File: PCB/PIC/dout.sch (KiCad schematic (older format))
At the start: 67 parts, among them J10 TB_1X3, J11 TB_1X2, J12 TB_1X3, J13 TB_1X3, J14 TB_1X2, J15 TB_1X3, K1 RELAY_G5V-2, K2 RELAY_G5V-2, K3 RELAY_G5V-2, K4 RELAY_G5V-2, Q11 NDS7002A, Q12 NDS7002A, Q2 FQT13N06L, Q3 FQT13N06L, Q4 FQT13N06L, Q5 FQT13N06L, Q6 NDS7002A, Q7 NDS7002A, U23 MCP1416, U27 MCP1416, U28 MCP1416, U29 MCP1416

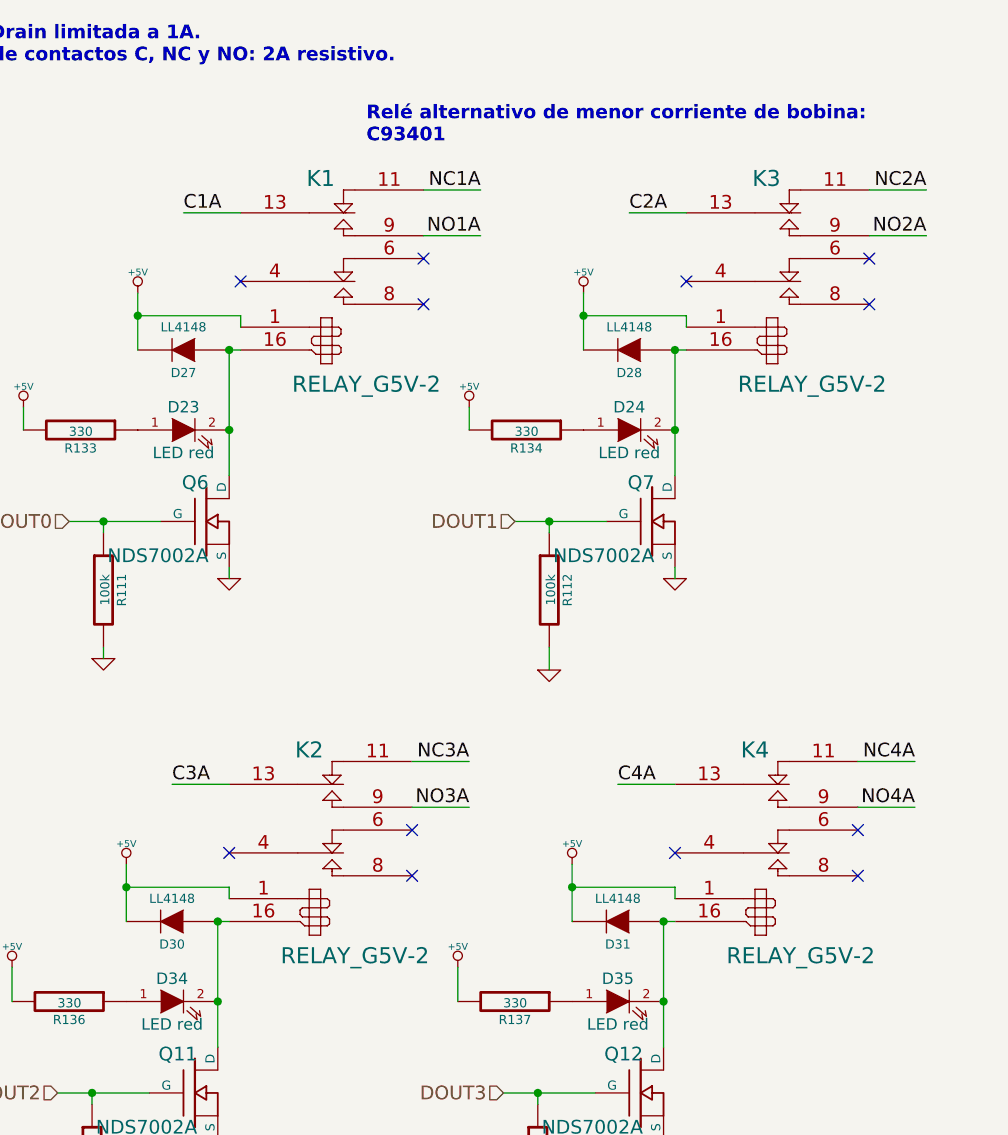
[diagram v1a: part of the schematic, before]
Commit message: cambio reles salida digital CIAA-PIC
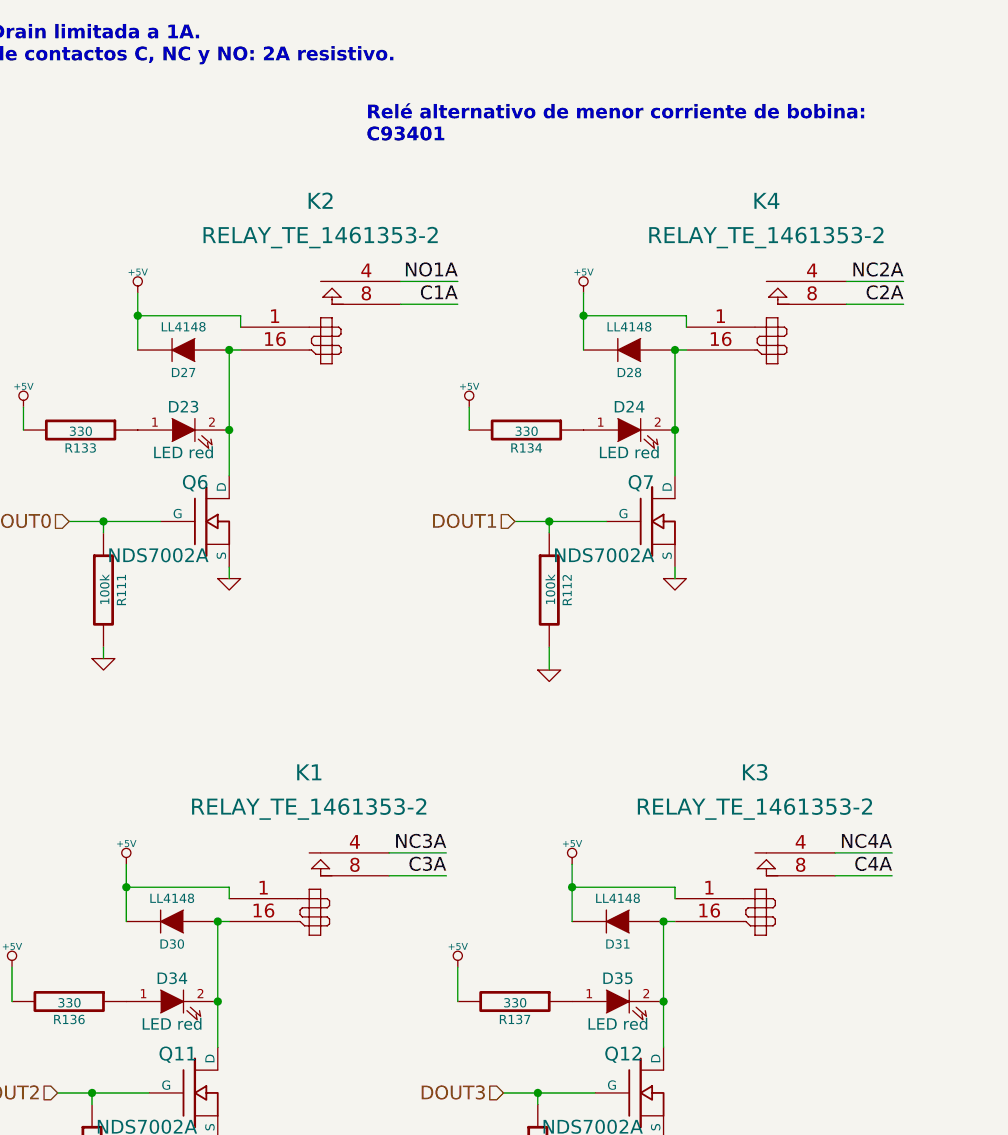
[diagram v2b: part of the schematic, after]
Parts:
- removed K1, K2, K3, K4: RELAY_G5V-2, footprints:G5V-2, symbol RELAY_G5V-2
- added K1, K2, K3, K4: RELAY_TE_1461353-2, footprints:1461353-2, symbol RELAY_TE_1461353-2
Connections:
- net +5V: now also K1.1, K2.1, K3.1, K4.1
- net C1A: now also K2.8 (T1)
- net C2A: now also K4.8 (T1)
- net C3A: now also K1.8 (T1)
- net C4A: now also K3.8 (T1)
- net NC2A: now also K4.4 (C1)
- net NC3A: now also K1.4 (C1)
- net NC4A: now also K3.4 (C1)
- net NO1A: now also K2.4 (C1)
- net at D23.2 (K), D27.1 (A), Q6.D: now also K2.16
- net at D30.1 (A), D34.2 (K), Q11.D: now also K1.16
- net at D24.2 (K), D28.1 (A), Q7.D: now also K4.16
- net at D31.1 (A), D35.2 (K), Q12.D: now also K3.16
- no-connect marks 12 -> 0
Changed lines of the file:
@@
 	0    -1   -1   0
 $EndComp
-Text Label 7650 1550 0    60   ~ 0
+Text Label 8850 1950 2    60   ~ 0
 C1A
-Text Label 8950 1450 2    60   ~ 0
-NC1A
-Text Label 8950 1650 2    60   ~ 0
+Text Label 8850 1850 2    60   ~ 0
 NO1A
 $Comp
@@
 	1    0    0    -1
 $EndComp
-Text Label 7600 4050 0    60   ~ 0
+Text Label 8800 4450 2    60   ~ 0
 C3A
-Text Label 8900 3950 2    60   ~ 0
+Text Label 8800 4350 2    60   ~ 0
 NC3A
-Text Label 8900 4150 2    60   ~ 0
-NO3A
 $Comp
 L MOSFET_N Q7
@@
 	1    0    0    -1
 $EndComp
-Text Label 9600 1550 0    60   ~ 0
+Text Label 10800 1950 2    60   ~ 0
 C2A
-Text Label 10900 1450 2    60   ~ 0
+Text Label 10800 1850 2    60   ~ 0
 NC2A
-Text Label 10900 1650 2    60   ~ 0
-NO2A
 $Comp
 L MOSFET_N Q12
@@
 	1    0    0    -1
 $EndComp
-Text Label 9550 4050 0    60   ~ 0
+Text Label 10750 4450 2    60   ~ 0
 C4A
-Text Label 10850 3950 2    60   ~ 0
+Text Label 10750 4350 2    60   ~ 0
 NC4A
-Text Label 10850 4150 2    60   ~ 0
-NO4A
 $Comp
 L THERMISTOR TH3
@@
 	3250 3200 3250 3150
 Wire Wire Line
-	7650 1550 7900 1550
-Wire Wire Line
-	8700 1450 8950 1450
-Wire Wire Line
-	8700 1650 8950 1650
+	8850 1950 8600 1950
+Wire Wire Line
+	8600 1850 8850 1850
 Wire Wire Line
 	7400 4400 7400 4650
@@
 Connection ~ 7250 5400
 Wire Wire Line
-	7600 4050 7850 4050
-Wire Wire Line
-	8650 3950 8900 3950
-Wire Wire Line
-	8650 4150 8900 4150
+	8800 4450 8550 4450
+Wire Wire Line
+	8550 4350 8800 4350
 Wire Wire Line
 	9400 1900 9400 2150
@@
 Connection ~ 9250 2900
 Wire Wire Line
-	9600 1550 9850 1550
-Wire Wire Line
-	10650 1450 10900 1450
-Wire Wire Line
-	10650 1650 10900 1650
+	10800 1950 10550 1950
+Wire Wire Line
+	10550 1850 10800 1850
 Wire Wire Line
 	9350 4400 9350 4650
@@
 Connection ~ 9200 5400
 Wire Wire Line
-	9550 4050 9800 4050
-Wire Wire Line
-	10600 3950 10850 3950
-Wire Wire Line
-	10600 4150 10850 4150
+	10750 4450 10500 4450
+Wire Wire Line
+	10500 4350 10750 4350
 Wire Wire Line
 	1050 5350 1750 5350
@@
 	1    0    0    -1
 $EndComp
-$Comp
-L RELAY_G5V-2 K1
-U 1 1 56AFD9BD
-P 8300 1800
-F 0 "K1" H 8250 2200 70  0000 C CNN
-F 1 "RELAY_G5V-2" H 8450 1300 70  0000 C CNN
-F 2 "footprints:G5V-2" H 7950 2300 60  0001 C CNN
-F 3 "http://www.digikey.hk/product-detail/en/omron-electronics-inc-emc-div/G5V-2-H1-DC24/Z110-ND/277846" H 8550 2550 60  0001 C CNN
-F 4 "G5V-2-DC5" H 8300 1800 60  0001 C CNN "manf#"
-	1    8300 1800
-	1    0    0    -1
-$EndComp
-$Comp
-L RELAY_G5V-2 K3
-U 1 1 56AFD9D4
-P 10250 1800
-F 0 "K3" H 10200 2200 70  0000 C CNN
-F 1 "RELAY_G5V-2" H 10400 1300 70  0000 C CNN
-F 2 "footprints:G5V-2" H 9650 2250 60  0001 C CNN
-F 3 "http://www.digikey.hk/product-detail/en/omron-electronics-inc-emc-div/G5V-2-H1-DC24/Z110-ND/277846" H 8550 2450 60  0001 C CNN
-F 4 "G5V-2-DC5" H 10250 1800 60  0001 C CNN "manf#"
-	1    10250 1800
-	1    0    0    -1
-$EndComp
-$Comp
-L RELAY_G5V-2 K4
-U 1 1 56AFD9E4
-P 10200 4300
-F 0 "K4" H 10150 4700 70  0000 C CNN
-F 1 "RELAY_G5V-2" H 10350 3800 70  0000 C CNN
-F 2 "footprints:G5V-2" H 10350 3700 60  0001 C CNN
-F 3 "http://www.digikey.hk/product-detail/en/omron-electronics-inc-emc-div/G5V-2-H1-DC24/Z110-ND/277846" H 8550 2150 60  0001 C CNN
-F 4 "G5V-2-DC5" H 10200 4300 60  0001 C CNN "manf#"
-	1    10200 4300
-	1    0    0    -1
-$EndComp
-$Comp
-L RELAY_G5V-2 K2
-U 1 1 56AFD9EA
-P 8250 4300
-F 0 "K2" H 8200 4700 70  0000 C CNN
-F 1 "RELAY_G5V-2" H 8400 3800 70  0000 C CNN
-F 2 "footprints:G5V-2" H 8400 3700 60  0001 C CNN
-F 3 "http://www.digikey.hk/product-detail/en/omron-electronics-inc-emc-div/G5V-2-H1-DC24/Z110-ND/277846" H 8550 2250 60  0001 C CNN
-F 4 "G5V-2-DC5" H 8250 4300 60  0001 C CNN "manf#"
-	1    8250 4300
-	1    0    0    -1
-$EndComp
 Wire Wire Line
 	7450 2000 7900 2000
@@
 Wire Wire Line
 	6900 4850 6900 5000
-NoConn ~ 8650 4250
-NoConn ~ 8650 4450
-NoConn ~ 10600 4250
-NoConn ~ 10600 4450
-NoConn ~ 7900 1850
-NoConn ~ 8700 1750
-NoConn ~ 8700 1950
-NoConn ~ 9850 1850
-NoConn ~ 10650 1750
-NoConn ~ 10650 1950
-NoConn ~ 7850 4350
-NoConn ~ 9800 4350
 Wire Wire Line
 	4000 1000 4000 2450
@@
 Wire Wire Line
 	4000 2450 4200 2450
+$Comp
+L RELAY_TE_1461353-2 K2
+U 1 1 57C69C4D
+P 8300 1800
+F 0 "K2" H 8250 2100 70  0000 C CNN
+F 1 "RELAY_TE_1461353-2" H 8250 1950 70  0000 C CNN
+F 2 "footprints:1461353-2" H 8200 1800 60  0001 C CNN
+F 3 "" H 8200 1800 60  0000 C CNN
+F 4 "1461353-2" H 8300 1800 60  0001 C CNN "manf#"
+	1    8300 1800
+	1    0    0    -1
+$EndComp
+$Comp
+L RELAY_TE_1461353-2 K4
+U 1 1 57C6B233
+P 10250 1800
+F 0 "K4" H 10200 2100 70  0000 C CNN
+F 1 "RELAY_TE_1461353-2" H 10200 1950 70  0000 C CNN
+F 2 "footprints:1461353-2" H 10150 1800 60  0001 C CNN
+F 3 "" H 10150 1800 60  0000 C CNN
+F 4 "1461353-2" H 10250 1800 60  0001 C CNN "manf#"
+	1    10250 1800
+	1    0    0    -1
+$EndComp
+$Comp
+L RELAY_TE_1461353-2 K3
+U 1 1 57C6BEA9
+P 10200 4300
+F 0 "K3" H 10150 4600 70  0000 C CNN
+F 1 "RELAY_TE_1461353-2" H 10150 4450 70  0000 C CNN
+F 2 "footprints:1461353-2" H 10100 4300 60  0001 C CNN
+F 3 "" H 10100 4300 60  0000 C CNN
+F 4 "1461353-2" H 10200 4300 60  0001 C CNN "manf#"
+	1    10200 4300
+	1    0    0    -1
+$EndComp
+$Comp
+L RELAY_TE_1461353-2 K1
+U 1 1 57C6C983
+P 8250 4300
+F 0 "K1" H 8200 4600 70  0000 C CNN
+F 1 "RELAY_TE_1461353-2" H 8200 4450 70  0000 C CNN
+F 2 "footprints:1461353-2" H 8150 4300 60  0001 C CNN
+F 3 "" H 8150 4300 60  0000 C CNN
+F 4 "1461353-2" H 8250 4300 60  0001 C CNN "manf#"
+	1    8250 4300
+	1    0    0    -1
+$EndComp
 $EndSCHEMATC

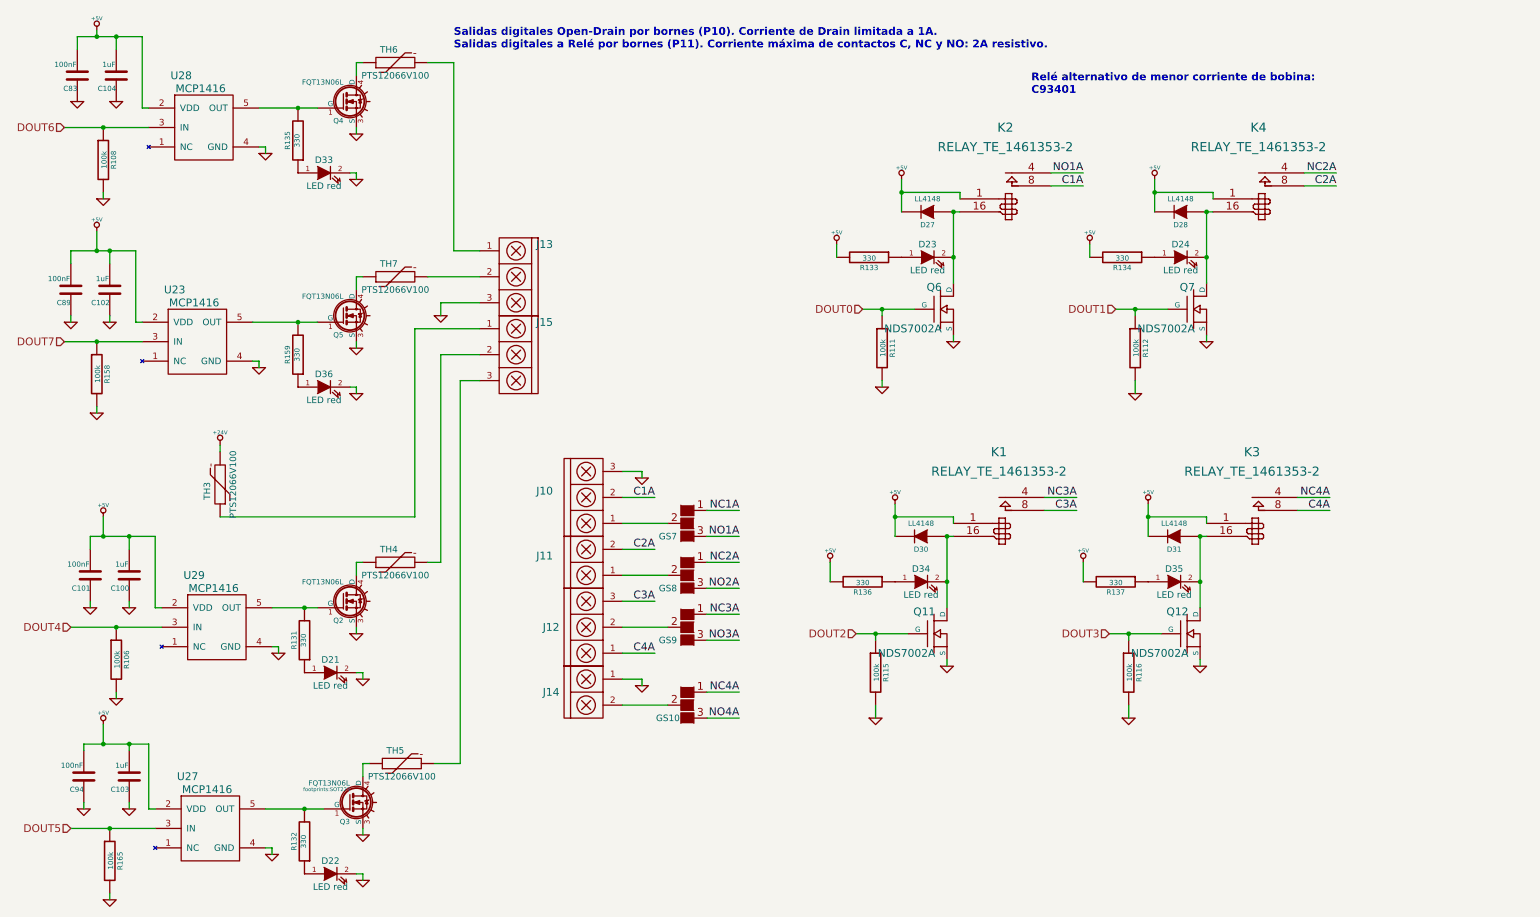
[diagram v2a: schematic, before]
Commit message: correccion masa rj45 CIAA-PIC
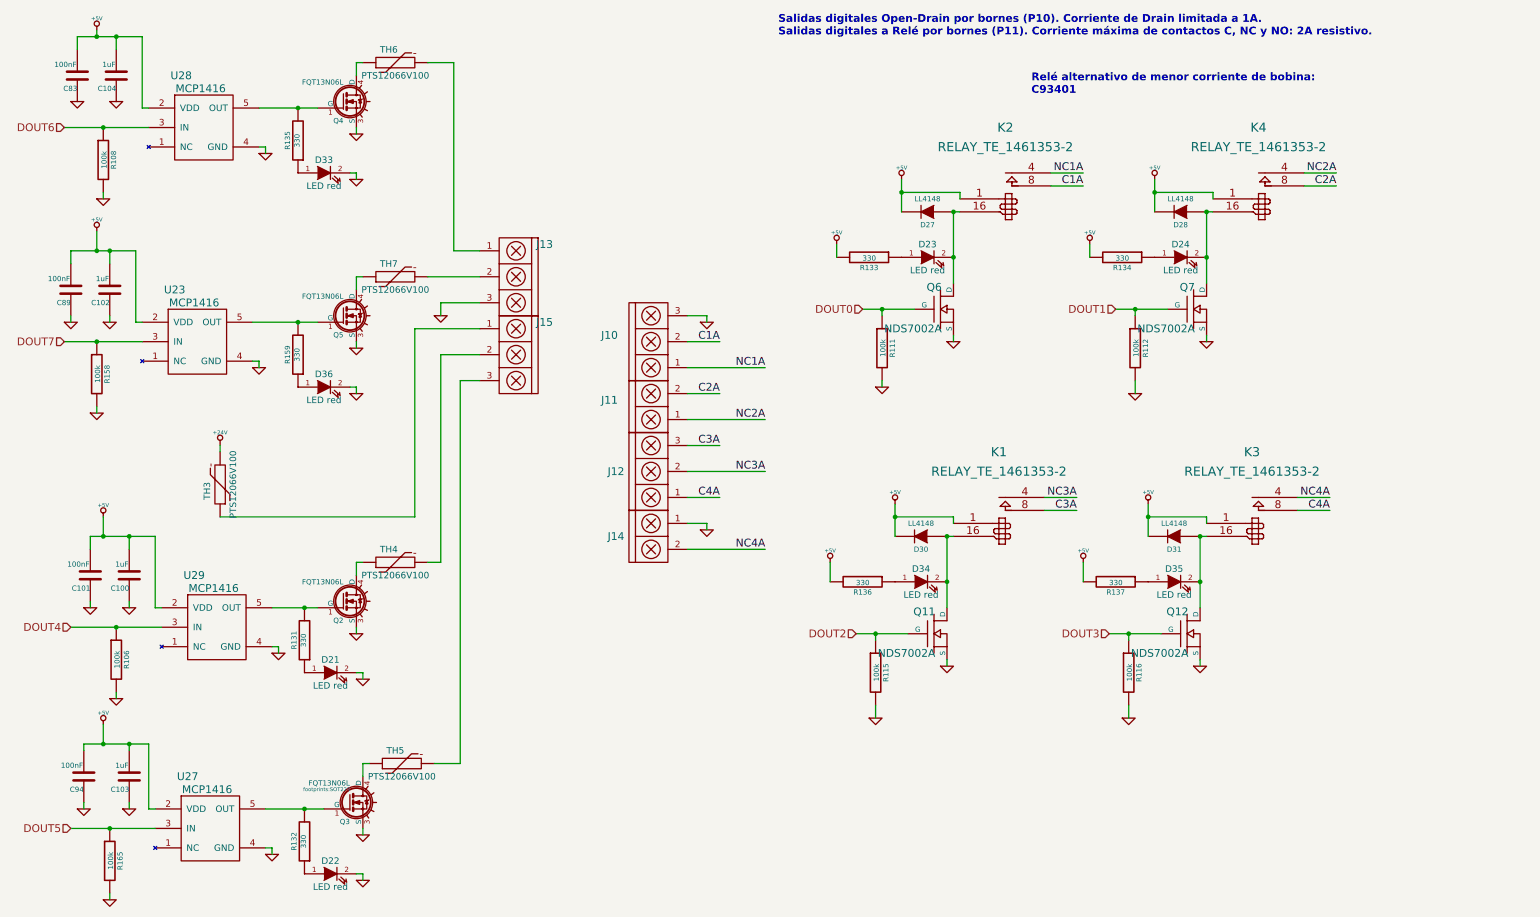
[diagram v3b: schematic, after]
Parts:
- removed GS10, GS7, GS8, GS9: GS3, footprints:GS3, symbol GS3
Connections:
- net NO1A is gone; now on net NC1A: K2.4 (C1)
- net NC1A: now also J10.1
- net NC2A: now also J11.1
- net NC3A: now also J12.2
- net NC4A: now also J14.2
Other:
- moved on the sheet: J10, J11, J12, J14

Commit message: correccion cristal FTDI,Moedlo RJ45 CIAA-PIC
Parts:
- TH3: footprint (none) -> footprints:MF-USMF

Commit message: completo BOM y pisadas
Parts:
- D27, D28, D30, D31: footprint (none) -> footprints:1n4148
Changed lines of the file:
@@
 F 0 "D27" H 7650 2250 40  0000 C CNN
 F 1 "LL4148" H 7650 2050 40  0000 C CNN
-F 2 "" H 7650 2150 60  0001 C CNN
+F 2 "footprints:1n4148" H 7650 2150 60  0001 C CNN
 F 3 "~" H 7650 2150 60  0000 C CNN
 F 4 "LL4148" H 7650 2150 60  0001 C CNN "manf#"
@@
 F 0 "D30" H 7600 4750 40  0000 C CNN
 F 1 "LL4148" H 7600 4550 40  0000 C CNN
-F 2 "" H 7600 4650 60  0001 C CNN
+F 2 "footprints:1n4148" H 7600 4650 60  0001 C CNN
 F 3 "~" H 7600 4650 60  0000 C CNN
 F 4 "LL4148" H 7600 4650 60  0001 C CNN "manf#"
@@
 F 0 "D28" H 9600 2250 40  0000 C CNN
 F 1 "LL4148" H 9600 2050 40  0000 C CNN
-F 2 "" H 9600 2150 60  0001 C CNN
+F 2 "footprints:1n4148" H 9600 2150 60  0001 C CNN
 F 3 "~" H 9600 2150 60  0000 C CNN
 F 4 "LL4148" H 9600 2150 60  0001 C CNN "manf#"
@@
 F 0 "D31" H 9550 4750 40  0000 C CNN
 F 1 "LL4148" H 9550 4550 40  0000 C CNN
-F 2 "" H 9550 4650 60  0001 C CNN
+F 2 "footprints:1n4148" H 9550 4650 60  0001 C CNN
 F 3 "~" H 9550 4650 60  0000 C CNN
 F 4 "LL4148" H 9550 4650 60  0001 C CNN "manf#"
